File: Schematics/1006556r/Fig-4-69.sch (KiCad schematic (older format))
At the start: 3 parts, among them J1 ConnectorGeneric, U901 D3NOR-+3VDC-0VDC-nd1021041-_3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, U902 D3NOR-NC-0VDC-expander-nd1021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

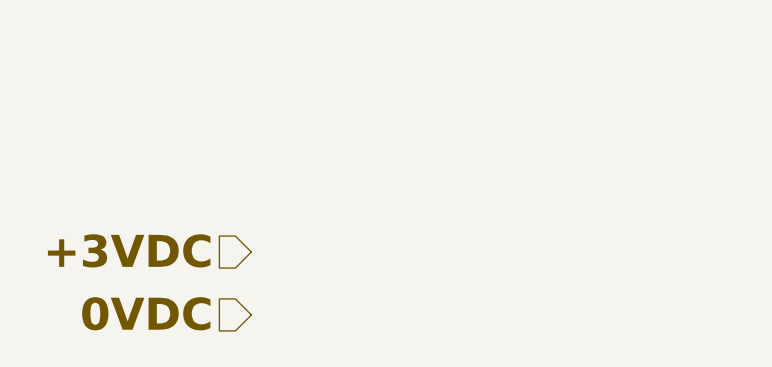
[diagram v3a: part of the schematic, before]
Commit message: Visual fixes were made using eelint, and some nominal electrical changes were made to accommodate current state of KiCad ERC capability. Nevertheless, ERC does not pass, due (I think) to current bugs in KiCad ERC.  Netlist changes are purely nominal, and relate to the addition of non-functional nodes in the power and ground nets.
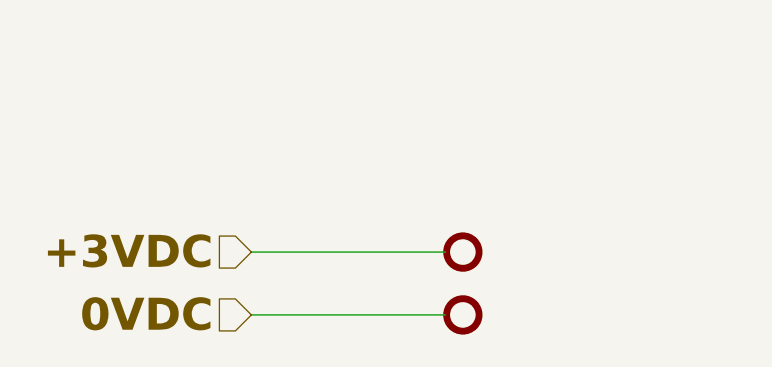
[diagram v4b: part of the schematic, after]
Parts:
- added N901, N902: Node2, symbol AGC_DSKY:Node2
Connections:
- net +3VDC: now also N901.1
- net 0VDC: now also N902.1
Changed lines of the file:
@@
-EESchema Schematic File Version 4
+EESchema Schematic File Version 5
 LIBS:module-cache
 EELAYER 29 0
@@
 Text HLabel 4325 4550 0    140  Input ~ 28
 g60039
+$Comp
+L AGC_DSKY:Node2 N?
+U 1 1 5CDF2013
+P 2525 7200
+AR Path="/5F3224B7/5CDF2013" Ref="N?"  Part="1"
+AR Path="/5F3224BF/5CDF2013" Ref="N901"  Part="1"
+F 0 "N901" H 2525 7300 50  0001 C CNN
+F 1 "Node2" H 2525 7375 50  0001 C CNN
+F 2 "" H 2525 7200 50  0001 C CNN
+F 3 "" H 2525 7200 50  0001 C CNN
+F 4 "+3VDC" H 2450 7200 140 0001 R CNB "Caption"
+	1    2525 7200
+	-1   0    0    1
+$EndComp
+$Comp
+L AGC_DSKY:Node2 N?
+U 1 1 5CDF201C
+P 2525 7475
+AR Path="/5F3224B7/5CDF201C" Ref="N?"  Part="0"
+AR Path="/5F3224BF/5CDF201C" Ref="N902"  Part="1"
+F 0 "N902" H 2525 7575 50  0001 C CNN
+F 1 "Node2" H 2525 7650 50  0001 C CNN
+F 2 "" H 2525 7475 50  0001 C CNN
+F 3 "" H 2525 7475 50  0001 C CNN
+F 4 "0VDC" H 2450 7475 140 0001 R CNB "Caption"
+	1    2525 7475
+	-1   0    0    1
+$EndComp
+Wire Wire Line
+	1600 7475 2450 7475
+Wire Wire Line
+	1600 7200 2450 7200
 $EndSCHEMATC
